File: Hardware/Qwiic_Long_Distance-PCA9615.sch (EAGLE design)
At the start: 33 parts, among them J3 RJ45_RJ11_COMBO, U1 PCA9615

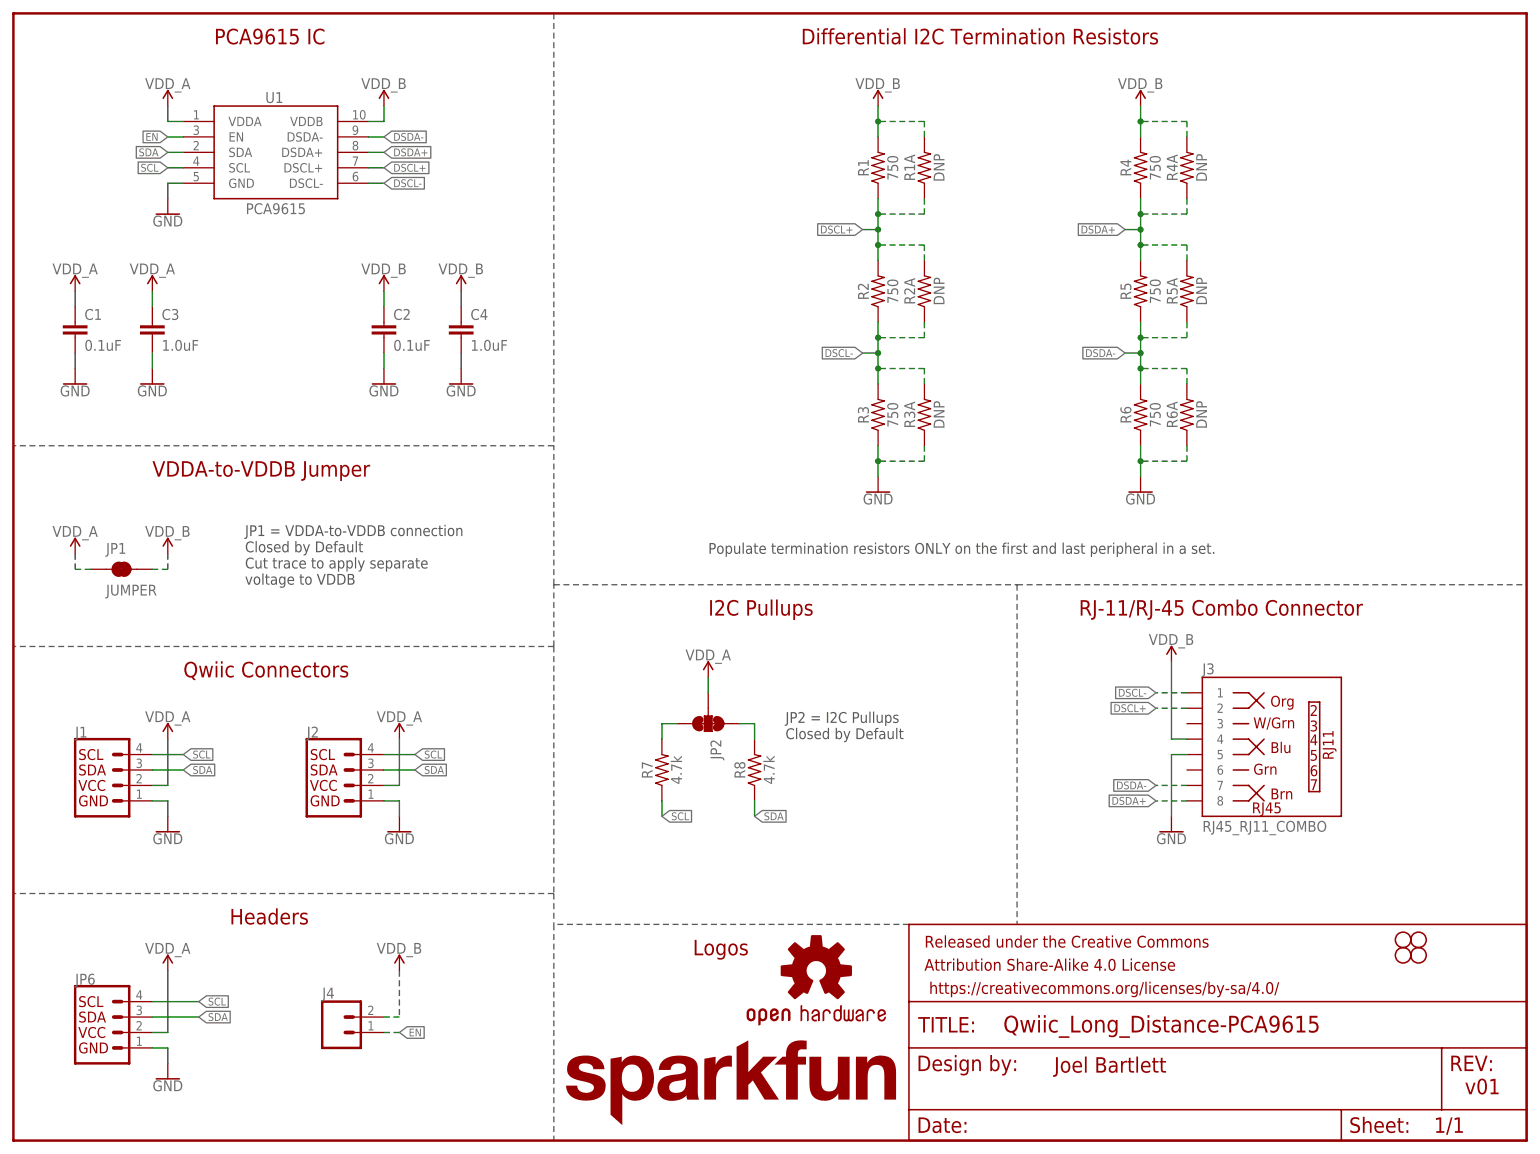
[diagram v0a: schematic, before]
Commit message: ENG Checklist update
Changes made after design review and ENG checklist.
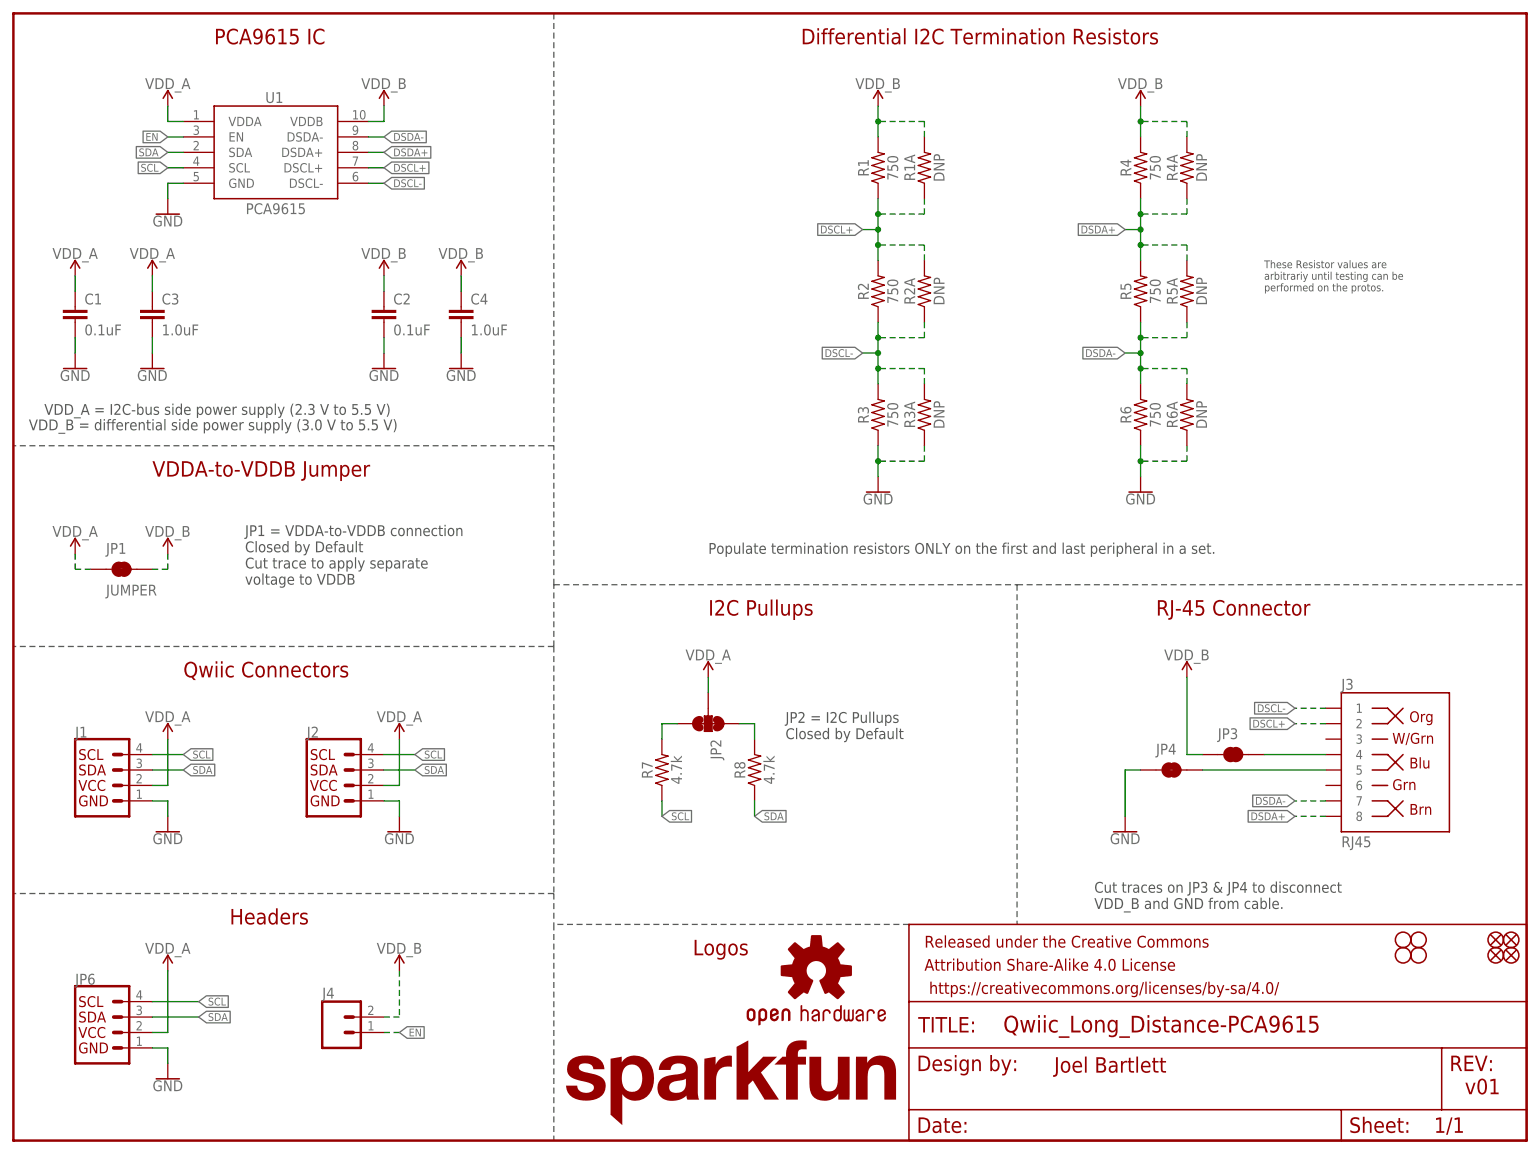
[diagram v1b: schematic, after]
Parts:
- added FD1, FD2, FD3, FD4: FIDUCIALUFIDUCIAL, SparkFun-Aesthetics:FIDUCIALUFIDUCIAL
- added JP3, JP4: JUMPER-SMT_2_NC_TRACE_SILK, SparkFun-Jumpers:JUMPER-SMT_2_NC_TRACE_SILK
- J3: value RJ45_RJ11_COMBO -> RJ45; device SparkX:RJ45_RJ11_COMBO -> SparkFun-Connectors:RJ45-8
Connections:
- new net N$1: J3.4, JP3.2
- new net N$2: J3.5, JP4.2
- net GND: now also JP4.1; no longer J3.5
- net VDD_B: now also JP3.1; no longer J3.4
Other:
- note added: "Cut traces on JP3 & JP4 to disconnect VDD_B and GND from cable."
- note added: "RJ-45 Connector"
- note added: "These Resistor values are arbitrariy until testing can be performed on the protos."
- note added: "VDD_A = I2C-bus side power supply (2.3 V to 5.5 V)"
- note added: "VDD_B = differential side power supply (3.0 V to 5.5 V)"
- note removed: "RJ-11/RJ-45 Combo Connector"
- moved on the sheet: C1, C2, C3, C4

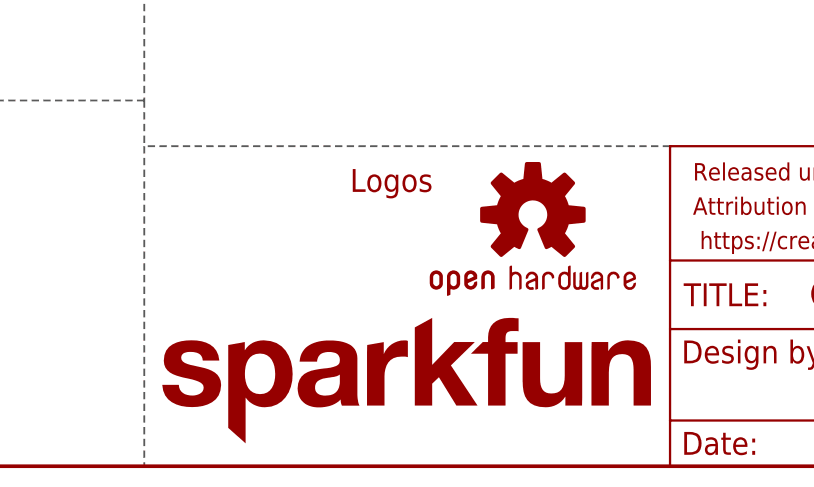
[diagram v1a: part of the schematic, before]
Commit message: Adding minor changes from QC checklist
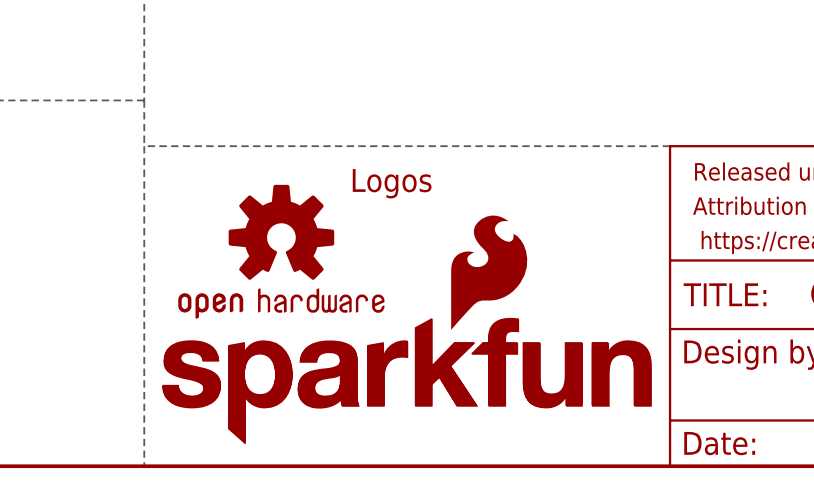
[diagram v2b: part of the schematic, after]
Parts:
- added LOGO5: SFE_LOGO_NAME_FLAME.1_INCH, SparkFun-Aesthetics:SFE_LOGO_NAME_FLAME.1_INCH
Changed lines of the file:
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@@
 <part name="FD3" library="SparkFun-Aesthetics" deviceset="FIDUCIAL" device="UFIDUCIAL"/>
 <part name="FD4" library="SparkFun-Aesthetics" deviceset="FIDUCIAL" device="UFIDUCIAL"/>
+<part name="LOGO5" library="SparkFun-Aesthetics" deviceset="SFE_LOGO_NAME_FLAME" device=".1_INCH"/>
 </parts>
 <sheets>
@@
 <instance part="SUPPLY14" gate="G$2" x="114.3" y="76.2"/>
 <instance part="LOGO2" gate="G$1" x="88.9" y="2.54"/>
-<instance part="LOGO1" gate="G$1" x="132.08" y="27.94"/>
+<instance part="LOGO1" gate="G$1" x="104.14" y="25.4"/>
 <instance part="JP3" gate="G$1" x="200.66" y="63.5"/>
 <instance part="JP4" gate="G$1" x="190.5" y="60.96"/>
@@
 <instance part="FD3" gate="G$1" x="243.84" y="33.02"/>
 <instance part="FD4" gate="G$1" x="243.84" y="30.48"/>
+<instance part="LOGO5" gate="G$1" x="90.17" y="2.032"/>
 </instances>
 <busses>
